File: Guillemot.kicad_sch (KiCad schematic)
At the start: 32 parts, among them Q1 IPB042N10N3G, Q2 AO3422, Q3 SI2309CDS, Q4 2N7002, Q5 MMBT3904, Q6 MMBT3904, U1 XIAO-nRF52840-SMD, U2 SN74LVC2G02DCTR

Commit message: Add PROTOCOL.md, Whimbrel provisioning, build fix (TinyUSB/SPI/bonding), config placeholders
Made-with: Cursor
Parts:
- added TP6: 3.3V, TestPoint:TestPoint_Pad_2.0x2.0mm, symbol Connector:TestPoint
- added TP7: GND, TestPoint:TestPoint_Pad_2.0x2.0mm, symbol Connector:TestPoint
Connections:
- net 3.3V: now also TP6.1
- net GND: now also TP7.1
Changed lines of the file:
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@@
 		)
 	)
+	(label "3.3V"
+		(at 134.62 137.16 270)
+		(effects
+			(font
+				(size 1.27 1.27)
+			)
+			(justify right bottom)
+		)
+	)
 	(label "PFET_CTRL"
 		(at 86.36 19.05 0)
@@
 	)
 	(symbol
+		(lib_id "power:GND")
+		(at 144.78 137.16 0)
+		(unit 1)
+		(exclude_from_sim no)
+		(in_bom yes)
+		(on_board yes)
+		(dnp no)
+		(fields_autoplaced yes)
+		(property "Reference" "#PWR07"
+			(at 144.78 143.51 0)
+			(effects
+				(font
+					(size 1.27 1.27)
+				)
+				(hide yes)
+			)
+		)
+		(property "Value" "GND"
+			(at 144.78 142.24 0)
+			(effects
+				(font
+					(size 1.27 1.27)
+				)
+			)
+		)
+		(property "Footprint" ""
+			(at 144.78 137.16 0)
+			(effects
+				(font
+					(size 1.27 1.27)
+				)
+				(hide yes)
+			)
+		)
+		(property "Datasheet" ""
+			(at 144.78 137.16 0)
+			(effects
+				(font
+					(size 1.27 1.27)
+				)
+				(hide yes)
+			)
+		)
+		(property "Description" "Power symbol creates a global label with name \"GND\" , ground"
+			(at 144.78 137.16 0)
+			(effects
+				(font
+					(size 1.27 1.27)
+				)
+				(hide yes)
+			)
+		)
+		(pin "1"
+		)
+		(instances
+			(project ""
+				(path "/024e03f0-ce48-4a1e-8a44-0ff4b1918b95"
+					(reference "#PWR07")
+					(unit 1)
+				)
+			)
+		)
+	)
+	(symbol
 		(lib_id "Device:C")
 		(at 180.34 49.53 90)
@@
 	)
 	(symbol
+		(lib_id "Connector:TestPoint")
+		(at 144.78 137.16 0)
+		(unit 1)
+		(exclude_from_sim no)
+		(in_bom yes)
+		(on_board yes)
+		(dnp no)
+		(fields_autoplaced yes)
+		(property "Reference" "TP7"
+			(at 147.32 132.5879 0)
+			(effects
+				(font
+					(size 1.27 1.27)
+				)
+				(justify left)
+			)
+		)
+		(property "Value" "GND"
+			(at 147.32 135.1279 0)
+			(effects
+				(font
+					(size 1.27 1.27)
+				)
+				(justify left)
+			)
+		)
+		(property "Footprint" "TestPoint:TestPoint_Pad_2.0x2.0mm"
+			(at 149.86 137.16 0)
+			(effects
+				(font
+					(size 1.27 1.27)
+				)
+				(hide yes)
+			)
+		)
+		(property "Datasheet" "~"
+			(at 149.86 137.16 0)
+			(effects
+				(font
+					(size 1.27 1.27)
+				)
+				(hide yes)
+			)
+		)
+		(property "Description" "test point"
+			(at 144.78 137.16 0)
+			(effects
+				(font
+					(size 1.27 1.27)
+				)
+				(hide yes)
+			)
+		)
+		(pin "1"
+		)
+		(instances
+			(project ""
+				(path "/024e03f0-ce48-4a1e-8a44-0ff4b1918b95"
+					(reference "TP7")
+					(unit 1)
+				)
+			)
+		)
+	)
+	(symbol
 		(lib_id "power:GND")
 		(at 194.31 105.41 90)
@@
 					(unit 1)
 				)
+			)
+		)
+	)
+	(symbol
+		(lib_id "Connector:TestPoint")
+		(at 134.62 137.16 0)
+		(unit 1)
+		(exclude_from_sim no)
+		(in_bom yes)
+		(on_board yes)
+		(dnp no)
+		(fields_autoplaced yes)
+		(property "Reference" "TP6"
+			(at 137.16 132.5879 0)
+			(effects
+				(font
+					(size 1.27 1.27)
+				)
+				(justify left)
+			)
+		)
+		(property "Value" "3.3V"
+			(at 137.16 135.1279 0)
+			(effects
+				(font
+					(size 1.27 1.27)
+				)
+				(justify left)
+			)
+		)
+		(property "Footprint" "TestPoint:TestPoint_Pad_2.0x2.0mm"
+			(at 139.7 137.16 0)
+			(effects
+				(font
+					(size 1.27 1.27)
+				)
+				(hide yes)
+			)
+		)
+		(property "Datasheet" "~"
+			(at 139.7 137.16 0)
+			(effects
+				(font
+					(size 1.27 1.27)
+				)
+				(hide yes)
+			)
+		)
+		(property "Description" "test point"
+			(at 134.62 137.16 0)
+			(effects
+				(font
+					(size 1.27 1.27)
+				)
+				(hide yes)
+			)
+		)
+		(pin "1"
+		)
+		(instances
+			(project ""
+				(path "/024e03f0-ce48-4a1e-8a44-0ff4b1918b95"
+					(reference "TP6")
+					(unit 1)
+				)

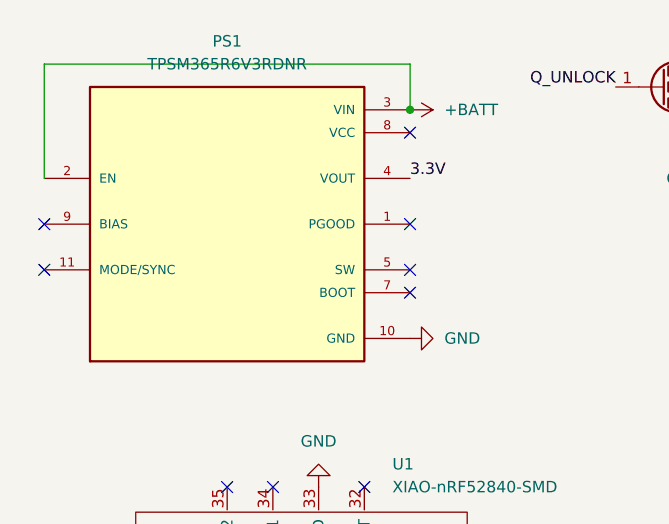
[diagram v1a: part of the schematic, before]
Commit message: Update KiCad project, README, production outputs; add fix_readme_cost.py
Made-with: Cursor
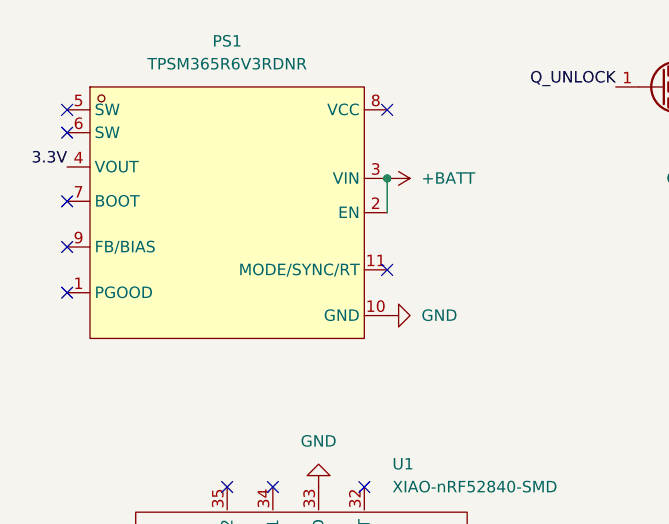
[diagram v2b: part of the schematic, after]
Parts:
- D4: LCSC Part C2099 -> C81598
- PS1: footprint TPSM365R6V3RDNR:CONV_TPSM365R6V3RDNR -> easyeda2kicad:QFN-11_L4.5-W3.5-P0.50-TL_TPSM365R6FRDNR; symbol TPSM365R6V3RDNR:TPSM365R6V3RDNR -> easyeda2kicad:TPSM365R6V3RDNR
- TP1, TP2, TP3, TP4: footprint TestPoint:TestPoint_Pad_4.0x4.0mm -> TestPoint:TestPoint_Pad_6.0x6.0mm
- TP5: footprint TestPoint:TestPoint_Pad_3.0x3.0mm -> TestPoint:TestPoint_Pad_4.0x4.0mm
- TP6, TP7: footprint TestPoint:TestPoint_Pad_2.0x2.0mm -> TestPoint:TestPoint_Pad_4.0x4.0mm
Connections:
- net at PS1.5 (SW): no longer PS1.6 (SW)
- no-connect marks 21 -> 22
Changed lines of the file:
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@@
 	(paper "A4")
 	(junction
-		(at 55.88 26.67)
+		(at 53.34 34.29)
 		(diameter 0)
 		(color 0 0 0 0)
@@
 	)
 	(no_connect
-		(at 15.24 44.45)
+		(at 17.78 46.99)
 	)
 	(no_connect
-		(at 55.88 29.21)
+		(at 53.34 26.67)
 	)
 	(no_connect
@@
 	)
 	(no_connect
-		(at 15.24 39.37)
+		(at 17.78 41.91)
 	)
 	(no_connect
@@
 	)
 	(no_connect
-		(at 55.88 44.45)
+		(at 17.78 29.21)
 	)
 	(no_connect
-		(at 55.88 39.37)
+		(at 53.34 44.45)
+	)
+	(no_connect
+		(at 17.78 36.83)
 	)
 	(no_connect
@@
 	)
 	(no_connect
-		(at 55.88 46.99)
+		(at 17.78 26.67)
 	)
 	(no_connect
@@
 	(wire
 		(pts
-			(xy 55.88 21.59) (xy 55.88 26.67)
-		)
-		(stroke
-			(width 0)
-			(type default)
-		)
-	)
-	(wire
-		(pts
 			(xy 20.32 101.6) (xy 22.86 101.6)
 		)
@@
 	(wire
 		(pts
-			(xy 15.24 34.29) (xy 15.24 21.59)
-		)
-		(stroke
-			(width 0)
-			(type default)
-		)
-	)
-	(wire
-		(pts
 			(xy 115.57 81.28) (xy 115.57 83.82)
 		)
@@
 	(wire
 		(pts
-			(xy 64.77 109.22) (xy 67.31 109.22)
+			(xy 53.34 34.29) (xy 53.34 38.1)
 		)
 		(stroke
@@
 	(wire
 		(pts
-			(xy 64.77 105.41) (xy 67.31 105.41)
+			(xy 64.77 109.22) (xy 67.31 109.22)
 		)
 		(stroke
@@
 	(wire
 		(pts
-			(xy 15.24 21.59) (xy 55.88 21.59)
+			(xy 64.77 105.41) (xy 67.31 105.41)
 		)
 		(stroke
@@
 	)
 	(label "3.3V"
-		(at 55.88 34.29 0)
+		(at 17.78 33.02 180)
 		(effects
 			(font
 				(size 1.27 1.27)
 			)
-			(justify left bottom)
+			(justify right bottom)
 		)
 	)
@@
 			)
 		)
-		(property "Footprint" "TestPoint:TestPoint_Pad_3.0x3.0mm"
+		(property "Footprint" "TestPoint:TestPoint_Pad_4.0x4.0mm"
 			(at 129.54 137.16 0)
 			(effects
@@
 			)
 		)
-		(property "Footprint" "TestPoint:TestPoint_Pad_4.0x4.0mm"
+		(property "Footprint" "TestPoint:TestPoint_Pad_6.0x6.0mm"
 			(at 119.38 137.16 0)
 			(effects
@@
 			)
 		)
-		(property "Footprint" "TestPoint:TestPoint_Pad_4.0x4.0mm"
+		(property "Footprint" "TestPoint:TestPoint_Pad_6.0x6.0mm"
 			(at 109.22 137.16 0)
 			(effects
@@
 			)
 		)
-		(property "LCSC Part" "C2099"
+		(property "LCSC Part" "C81598"
 			(at 254 71.12 0)
 			(effects
@@
 	)
 	(symbol
-		(lib_id "TPSM365R6V3RDNR:TPSM365R6V3RDNR")
+		(lib_id "easyeda2kicad:TPSM365R6V3RDNR")
 		(at 35.56 39.37 0)
 		(unit 1)
@@
 			)
 		)
-		(property "Footprint" "TPSM365R6V3RDNR:CONV_TPSM365R6V3RDNR"
-			(at 35.56 39.37 0)
+		(property "Footprint" "easyeda2kicad:QFN-11_L4.5-W3.5-P0.50-TL_TPSM365R6FRDNR"
+			(at 35.56 57.15 0)
 			(effects
 				(font
 					(size 1.27 1.27)
 				)
-				(justify bottom)
 				(hide yes)
 			)
@@
 		)
 		(property "LCSC Part" "C18208843"
-			(at 35.56 39.37 0)
+			(at 35.56 59.69 0)
 			(effects
 				(font
@@
 			)
 		)
-		(property "Footprint" "TestPoint:TestPoint_Pad_4.0x4.0mm"
+		(property "Footprint" "TestPoint:TestPoint_Pad_6.0x6.0mm"
 			(at 100.33 137.16 0)
 			(effects
@@
 	(symbol
 		(lib_id "power:GND")
-		(at 55.88 52.07 90)
+		(at 53.34 49.53 90)
 		(unit 1)
 		(exclude_from_sim no)
@@
 		(fields_autoplaced yes)
 		(property "Reference" "#PWR02"
-			(at 62.23 52.07 0)
+			(at 59.69 49.53 0)
 			(effects
 				(font
@@
 		)
 		(property "Value" "GND"
-			(at 59.69 52.0699 90)
+			(at 57.15 49.5299 90)
 			(effects
 				(font
@@
 		)
 		(property "Footprint" ""
-			(at 55.88 52.07 0)
+			(at 53.34 49.53 0)
 			(effects
 				(font
@@
 		)
 		(property "Datasheet" ""
-			(at 55.88 52.07 0)
+			(at 53.34 49.53 0)
 			(effects
 				(font
@@
 		)
 		(property "Description" "Power symbol creates a global label with name \"GND\" , ground"
-			(at 55.88 52.07 0)
+			(at 53.34 49.53 0)
 			(effects
 				(font
@@
 			)
 		)
-		(property "Footprint" "TestPoint:TestPoint_Pad_2.0x2.0mm"
+		(property "Footprint" "TestPoint:TestPoint_Pad_4.0x4.0mm"
 			(at 149.86 137.16 0)
 			(effects
@@
 			)
 		)
-		(property "Footprint" "TestPoint:TestPoint_Pad_4.0x4.0mm"
+		(property "Footprint" "TestPoint:TestPoint_Pad_6.0x6.0mm"
 			(at 90.17 137.16 0)
 			(effects
@@
 	(symbol
 		(lib_id "power:+BATT")
-		(at 55.88 26.67 270)
+		(at 53.34 34.29 270)
 		(unit 1)
 		(exclude_from_sim no)
@@
 		(fields_autoplaced yes)
 		(property "Reference" "#PWR01"
-			(at 52.07 26.67 0)
+			(at 49.53 34.29 0)
 			(effects
 				(font
@@
 		)
 		(property "Value" "+BATT"
-			(at 59.69 26.6699 90)
+			(at 57.15 34.2899 90)
 			(effects
 				(font
@@
 		)
 		(property "Footprint" ""
-			(at 55.88 26.67 0)
+			(at 53.34 34.29 0)
 			(effects
 				(font
@@
 		)
 		(property "Datasheet" ""
-			(at 55.88 26.67 0)
+			(at 53.34 34.29 0)
 			(effects
 				(font
@@
 		)
 		(property "Description" "Power symbol creates a global label with name \"+BATT\""
-			(at 55.88 26.67 0)
+			(at 53.34 34.29 0)
 			(effects
 				(font
@@
 			)
 		)
-		(property "Footprint" "TestPoint:TestPoint_Pad_2.0x2.0mm"
+		(property "Footprint" "TestPoint:TestPoint_Pad_4.0x4.0mm"
 			(at 139.7 137.16 0)
 			(effects

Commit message: docs: add architecture critique, update readme and pcb files
Made-with: Cursor
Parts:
- D3: LCSC Part C2099 -> C81598
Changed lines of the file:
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@@
 			)
 		)
-		(property "LCSC Part" "C2099"
+		(property "LCSC Part" "C81598"
 			(at 254 25.4 0)
 			(effects
